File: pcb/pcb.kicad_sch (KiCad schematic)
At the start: 0 parts

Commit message: usbc almost done
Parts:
- added J1: TYPE-C-31-M-31, Andrews_Library:LCSC_SMD_USBC_C2760486, symbol Andrews_Library:LCSC_SMD_USBC_C2760486
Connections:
- no-connect marks 0 -> 13
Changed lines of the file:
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@@
 		(company "Andrew Cromar")
+	)
+	(no_connect
+		(at 139.7 88.9)
+	)
+	(no_connect
+		(at 128.27 80.01)
+	)
+	(no_connect
+		(at 130.81 106.68)
+	)
+	(no_connect
+		(at 128.27 106.68)
+	)
+	(no_connect
+		(at 139.7 93.98)
+	)
+	(no_connect
+		(at 139.7 96.52)
+	)
+	(no_connect
+		(at 139.7 99.06)
+	)
+	(no_connect
+		(at 139.7 91.44)
+	)
+	(no_connect
+		(at 125.73 106.68)
+	)
+	(no_connect
+		(at 139.7 86.36)
+	)
+	(no_connect
+		(at 116.84 99.06)
+	)
+	(no_connect
+		(at 130.81 80.01)
+	)
+	(no_connect
+		(at 116.84 96.52)
+	)
+	(symbol
+		(lib_id "Andrews_Library:LCSC_SMD_USBC_C2760486")
+		(at 128.27 92.71 0)
+		(unit 1)
+		(body_style 1)
+		(exclude_from_sim no)
+		(in_bom yes)
+		(on_board yes)
+		(in_pos_files yes)
+		(dnp no)
+		(fields_autoplaced yes)
+		(property "Reference" "J1"
+			(at 132.9533 77.47 0)
+			(show_name no)
+			(do_not_autoplace no)
+			(effects
+				(font
+					(size 1.27 1.27)
+				)
+				(justify left)
+			)
+		)
+		(property "Value" "TYPE-C-31-M-31"
+			(at 132.9533 80.01 0)
+			(show_name no)
+			(do_not_autoplace no)
+			(effects
+				(font
+					(size 1.27 1.27)
+				)
+				(justify left)
+			)
+		)
+		(property "Footprint" "Andrews_Library:LCSC_SMD_USBC_C2760486"
+			(at 128.27 92.71 0)
+			(hide yes)
+			(show_name no)
+			(do_not_autoplace no)
+			(effects
+				(font
+					(size 1.27 1.27)
+				)
+			)
+		)
+		(property "Datasheet" "https://www.lcsc.com/datasheet/C2760486.pdf"
+			(at 128.27 92.71 0)
+			(hide yes)
+			(show_name no)
+			(do_not_autoplace no)
+			(effects
+				(font
+					(size 1.27 1.27)
+				)
+			)
+		)
+		(property "Description" ""
+			(at 128.27 92.71 0)
+			(hide yes)
+			(show_name no)
+			(do_not_autoplace no)
+			(effects
+				(font
+					(size 1.27 1.27)
+				)
+			)
+		)
+		(property "LCSC" "C2760486"
+			(at 128.27 92.71 0)
+			(hide yes)
+			(show_name no)
+			(do_not_autoplace no)
+			(effects
+				(font
+					(size 1.27 1.27)
+				)
+			)
+		)
+		(pin "A12"
+		)
+		(pin "B8"
+		)
+		(pin "A7"
+		)
+		(pin "A8"
+		)
+		(pin "A9"
+		)
+		(pin "B7"
+		)
+		(pin "B5"
+		)
+		(pin "B6"
+		)
+		(pin "A6"
+		)
+		(pin "A5"
+		)
+		(pin "A4"
+		)
+		(pin "A1"
+		)
+		(pin "1"
+		)
+		(instances
+			(project "pcb"
+				(path "/37969d75-6775-4969-b3c5-2af34bbf809f"
+					(reference "J1")
+					(unit 1)
+				)
+			)
+		)
 	)
 	(sheet_instances

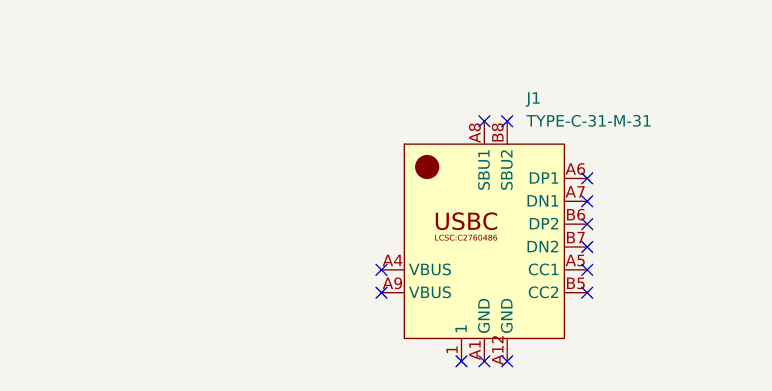
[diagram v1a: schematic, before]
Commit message: started working on voltage regulator
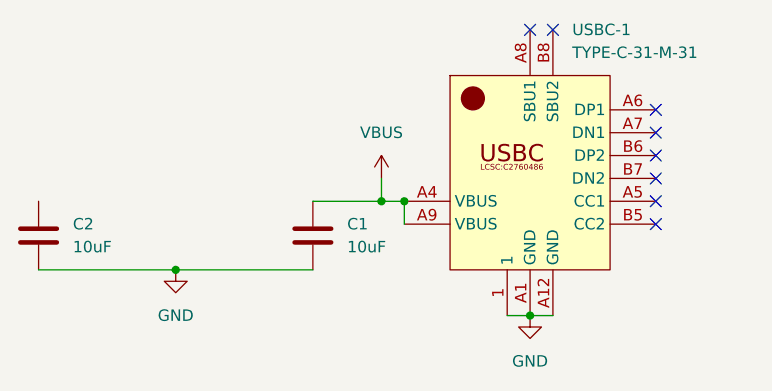
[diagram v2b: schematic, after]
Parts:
- removed J1: TYPE-C-31-M-31, Andrews_Library:LCSC_SMD_USBC_C2760486, symbol Andrews_Library:LCSC_SMD_USBC_C2760486
- added C1, C2: 10uF, symbol Device:C
- added USBC-1: TYPE-C-31-M-31, Andrews_Library:LCSC_SMD_USBC_C2760486, symbol Andrews_Library:LCSC_SMD_USBC_C2760486
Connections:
- new net GND: C1.2, C2.2, USBC-1.1, USBC-1.A1 (GND), USBC-1.A12 (GND)
- new net VBUS: C1.1, USBC-1.A4 (VBUS), USBC-1.A9 (VBUS)
- no-connect marks 13 -> 8

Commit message: please
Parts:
- added U1: 1117-3.3, symbol Andrews_Library:LCSC_SMD_1117-3.3v_C5125088
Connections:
- net GND: now also C1.1, U1.1 (GND/ADJ); no longer C1.2
- net VBUS: now also C1.2, U1.3 (VIN); no longer C1.1
- net at C2.1: now also U1.2 (VOUT), U1.4 (VOUT)
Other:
- moved on the sheet: C1, C2
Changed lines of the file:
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@@
+	)
+	(junction
+		(at 87.63 88.9)
+		(diameter 0)
+		(color 0 0 0 0)
+	)
+	(junction
+		(at 114.3 88.9)
+		(diameter 0)
+		(color 0 0 0 0)
 	)
 	(junction
@@
 	)
 	(junction
-		(at 93.98 96.52)
+		(at 97.79 96.52)
 		(diameter 0)
 		(color 0 0 0 0)
@@
 	(wire
 		(pts
-			(xy 93.98 96.52) (xy 109.22 96.52)
-		)
-		(stroke
-			(width 0)
-			(type default)
-		)
-	)
-	(wire
-		(pts
-			(xy 109.22 88.9) (xy 116.84 88.9)
-		)
-		(stroke
-			(width 0)
-			(type default)
-		)
-	)
-	(wire
-		(pts
-			(xy 119.38 88.9) (xy 116.84 88.9)
+			(xy 114.3 88.9) (xy 116.84 88.9)
+		)
+		(stroke
+			(width 0)
+			(type default)
+		)
+	)
+	(wire
+		(pts
+			(xy 97.79 96.52) (xy 114.3 96.52)
+		)
+		(stroke
+			(width 0)
+			(type default)
+		)
+	)
+	(wire
+		(pts
+			(xy 87.63 88.9) (xy 87.63 90.17)
+		)
+		(stroke
+			(width 0)
+			(type default)
+		)
+	)
+	(wire
+		(pts
+			(xy 87.63 87.63) (xy 87.63 88.9)
+		)
+		(stroke
+			(width 0)
+			(type default)
+		)
+	)
+	(wire
+		(pts
+			(xy 80.01 88.9) (xy 87.63 88.9)
+		)
+		(stroke
+			(width 0)
+			(type default)
+		)
+	)
+	(wire
+		(pts
+			(xy 97.79 93.98) (xy 97.79 96.52)
+		)
+		(stroke
+			(width 0)
+			(type default)
+		)
+	)
+	(wire
+		(pts
+			(xy 116.84 88.9) (xy 119.38 88.9)
 		)
 		(stroke
@@
 	(wire
 		(pts
-			(xy 78.74 96.52) (xy 93.98 96.52)
+			(xy 80.01 96.52) (xy 97.79 96.52)
+		)
+		(stroke
+			(width 0)
+			(type default)
+		)
+	)
+	(wire
+		(pts
+			(xy 106.68 88.9) (xy 114.3 88.9)
 		)
 		(stroke
@@
 	)
 	(symbol
+		(lib_id "Andrews_Library:LCSC_SMD_1117-3.3v_C5125088")
+		(at 97.79 83.82 0)
+		(mirror y)
+		(unit 1)
+		(body_style 1)
+		(exclude_from_sim no)
+		(in_bom yes)
+		(on_board yes)
+		(in_pos_files yes)
+		(dnp no)
+		(fields_autoplaced yes)
+		(property "Reference" "U1"
+			(at 97.155 71.12 0)
+			(show_name no)
+			(do_not_autoplace no)
+			(effects
+				(font
+					(size 1.27 1.27)
+				)
+			)
+		)
+		(property "Value" "1117-3.3"
+			(at 97.155 73.66 0)
+			(show_name no)
+			(do_not_autoplace no)
+			(effects
+				(font
+					(size 1.27 1.27)
+				)
+			)
+		)
+		(property "Footprint" ""
+			(at 101.6 78.74 0)
+			(hide yes)
+			(show_name no)
+			(do_not_autoplace no)
+			(effects
+				(font
+					(size 1.27 1.27)
+				)
+			)
+		)
+		(property "Datasheet" "https://www.lcsc.com/datasheet/C5125088.pdf"
+			(at 97.79 83.82 0)
+			(hide yes)
+			(show_name no)
+			(do_not_autoplace no)
+			(effects
+				(font
+					(size 1.27 1.27)
+				)
+			)
+		)
+		(property "Description" ""
+			(at 101.6 78.74 0)
+			(hide yes)
+			(show_name no)
+			(do_not_autoplace no)
+			(effects
+				(font
+					(size 1.27 1.27)
+				)
+			)
+		)
+		(property "LCSC" "C5125088"
+			(at 97.79 83.82 0)
+			(hide yes)
+			(show_name no)
+			(do_not_autoplace no)
+			(effects
+				(font
+					(size 1.27 1.27)
+				)
+			)
+		)
+		(pin "1"
+		)
+		(pin "4"
+		)
+		(pin "3"
+		)
+		(pin "2"
+		)
+		(instances
+			(project "pcb"
+				(path "/37969d75-6775-4969-b3c5-2af34bbf809f"
+					(reference "U1")
+					(unit 1)
+				)
+			)
+		)
+	)
+	(symbol
 		(lib_id "power:GND")
 		(at 133.35 101.6 0)
@@
 	(symbol
 		(lib_id "Device:C")
-		(at 109.22 92.71 0)
+		(at 114.3 92.71 0)
+		(mirror x)
 		(unit 1)
 		(body_style 1)
@@
 		(in_pos_files yes)
 		(dnp no)
-		(fields_autoplaced yes)
 		(property "Reference" "C1"
-			(at 113.03 91.4399 0)
-			(show_name no)
-			(do_not_autoplace no)
-			(effects
-				(font
-					(size 1.27 1.27)
-				)
-				(justify left)
+			(at 110.49 91.4399 0)
+			(show_name no)
+			(do_not_autoplace no)
+			(effects
+				(font
+					(size 1.27 1.27)
+				)
+				(justify right)
 			)
 		)
 		(property "Value" "10uF"
-			(at 113.03 93.9799 0)
-			(show_name no)
-			(do_not_autoplace no)
-			(effects
-				(font
-					(size 1.27 1.27)
-				)
-				(justify left)
+			(at 110.49 93.9799 0)
+			(show_name no)
+			(do_not_autoplace no)
+			(effects
+				(font
+					(size 1.27 1.27)
+				)
+				(justify right)
 			)
 		)
 		(property "Footprint" ""
-			(at 110.1852 96.52 0)
+			(at 115.2652 88.9 0)
 			(hide yes)
 			(show_name no)
@@
 		)
 		(property "Datasheet" ""
-			(at 109.22 92.71 0)
+			(at 114.3 92.71 0)
 			(hide yes)
 			(show_name no)
@@
 		)
 		(property "Description" "Unpolarized capacitor"
-			(at 109.22 92.71 0)
+			(at 114.3 92.71 0)
 			(hide yes)
 			(show_name no)
@@
 	(symbol
 		(lib_id "power:GND")
-		(at 93.98 96.52 0)
+		(at 97.79 96.52 0)
 		(unit 1)
 		(body_style 1)
@@
 		(fields_autoplaced yes)
 		(property "Reference" "#PWR03"
-			(at 93.98 102.87 0)
+			(at 97.79 102.87 0)
 			(hide yes)
 			(show_name no)
@@
 		)
 		(property "Value" "GND"
-			(at 93.98 101.6 0)
+			(at 97.79 101.6 0)
 			(show_name no)
 			(do_not_autoplace no)
@@
 		)
 		(property "Footprint" ""
-			(at 93.98 96.52 0)
+			(at 97.79 96.52 0)
 			(hide yes)
 			(show_name no)
@@
 		)
 		(property "Datasheet" ""
-			(at 93.98 96.52 0)
+			(at 97.79 96.52 0)
 			(hide yes)
 			(show_name no)
@@
 		)
 		(property "Description" "Power symbol creates a global label with name \"GND\" , ground"
-			(at 93.98 96.52 0)
+			(at 97.79 96.52 0)
 			(hide yes)
 			(show_name no)
@@
 	(symbol
 		(lib_id "Device:C")
-		(at 78.74 92.71 0)
+		(at 80.01 92.71 0)
 		(unit 1)
 		(body_style 1)
@@
 		(fields_autoplaced yes)
 		(property "Reference" "C2"
-			(at 82.55 91.4399 0)
+			(at 83.82 91.4399 0)
 			(show_name no)
 			(do_not_autoplace no)
@@
 		)
 		(property "Value" "10uF"
-			(at 82.55 93.9799 0)
+			(at 83.82 93.9799 0)
 			(show_name no)
 			(do_not_autoplace no)
@@
 		)
 		(property "Footprint" ""
-			(at 79.7052 96.52 0)
+			(at 80.9752 96.52 0)
 			(hide yes)
 			(show_name no)
@@
 		)
 		(property "Datasheet" ""
-			(at 78.74 92.71 0)
+			(at 80.01 92.71 0)
 			(hide yes)
 			(show_name no)
@@
 		)
 		(property "Description" "Unpolarized capacitor"
-			(at 78.74 92.71 0)
-			(hide yes)
-			(show_name no)
+			(at 80.01 92.71 0)
+			(hide yes)
+			(show_name no)

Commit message: added it to the pcb
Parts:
- U1: footprint (none) -> Andrews_Library:LCSC_SMD_1117-3.3v_C5125088
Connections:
- net VBUS: now also U1.2 (VOUT); no longer U1.3 (VIN)
- new net: C2.1, U1.3 (VIN)
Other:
- moved on the sheet: C2
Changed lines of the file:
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@@
 	)
 	(junction
-		(at 87.63 88.9)
+		(at 119.38 88.9)
+		(diameter 0)
+		(color 0 0 0 0)
+	)
+	(junction
+		(at 97.79 96.52)
 		(diameter 0)
 		(color 0 0 0 0)
@@
 	)
 	(junction
-		(at 119.38 88.9)
-		(diameter 0)
-		(color 0 0 0 0)
-	)
-	(junction
-		(at 97.79 96.52)
-		(diameter 0)
-		(color 0 0 0 0)
-	)
-	(junction
 		(at 133.35 101.6)
 		(diameter 0)
@@
 	(wire
 		(pts
+			(xy 82.55 88.9) (xy 88.9 88.9)
+		)
+		(stroke
+			(width 0)
+			(type default)
+		)
+	)
+	(wire
+		(pts
 			(xy 130.81 101.6) (xy 133.35 101.6)
 		)
@@
 	(wire
 		(pts
-			(xy 87.63 88.9) (xy 87.63 90.17)
-		)
-		(stroke
-			(width 0)
-			(type default)
-		)
-	)
-	(wire
-		(pts
-			(xy 87.63 87.63) (xy 87.63 88.9)
-		)
-		(stroke
-			(width 0)
-			(type default)
-		)
-	)
-	(wire
-		(pts
-			(xy 80.01 88.9) (xy 87.63 88.9)
-		)
-		(stroke
-			(width 0)
-			(type default)
-		)
-	)
-	(wire
-		(pts
 			(xy 97.79 93.98) (xy 97.79 96.52)
 		)
@@
 	(wire
 		(pts
-			(xy 80.01 96.52) (xy 97.79 96.52)
-		)
-		(stroke
-			(width 0)
-			(type default)
-		)
-	)
-	(wire
-		(pts
-			(xy 106.68 88.9) (xy 114.3 88.9)
+			(xy 107.95 88.9) (xy 114.3 88.9)
+		)
+		(stroke
+			(width 0)
+			(type default)
+		)
+	)
+	(wire
+		(pts
+			(xy 82.55 96.52) (xy 97.79 96.52)
 		)
 		(stroke
@@
 	)
 	(symbol
-		(lib_id "Andrews_Library:LCSC_SMD_1117-3.3v_C5125088")
-		(at 97.79 83.82 0)
-		(mirror y)
-		(unit 1)
-		(body_style 1)
-		(exclude_from_sim no)
-		(in_bom yes)
-		(on_board yes)
-		(in_pos_files yes)
-		(dnp no)
-		(fields_autoplaced yes)
-		(property "Reference" "U1"
-			(at 97.155 71.12 0)
-			(show_name no)
-			(do_not_autoplace no)
-			(effects
-				(font
-					(size 1.27 1.27)
-				)
-			)
-		)
-		(property "Value" "1117-3.3"
-			(at 97.155 73.66 0)
-			(show_name no)
-			(do_not_autoplace no)
-			(effects
-				(font
-					(size 1.27 1.27)
-				)
-			)
-		)
-		(property "Footprint" ""
-			(at 101.6 78.74 0)
-			(hide yes)
-			(show_name no)
-			(do_not_autoplace no)
-			(effects
-				(font
-					(size 1.27 1.27)
-				)
-			)
-		)
-		(property "Datasheet" "https://www.lcsc.com/datasheet/C5125088.pdf"
-			(at 97.79 83.82 0)
-			(hide yes)
-			(show_name no)
-			(do_not_autoplace no)
-			(effects
-				(font
-					(size 1.27 1.27)
-				)
-			)
-		)
-		(property "Description" ""
-			(at 101.6 78.74 0)
-			(hide yes)
-			(show_name no)
-			(do_not_autoplace no)
-			(effects
-				(font
-					(size 1.27 1.27)
-				)
-			)
-		)
-		(property "LCSC" "C5125088"
-			(at 97.79 83.82 0)
-			(hide yes)
-			(show_name no)
-			(do_not_autoplace no)
-			(effects
-				(font
-					(size 1.27 1.27)
-				)
-			)
-		)
-		(pin "1"
-		)
-		(pin "4"
-		)
-		(pin "3"
-		)
-		(pin "2"
-		)
-		(instances
-			(project "pcb"
-				(path "/37969d75-6775-4969-b3c5-2af34bbf809f"
-					(reference "U1")
-					(unit 1)
-				)
-			)
-		)
-	)
-	(symbol
 		(lib_id "power:GND")
 		(at 133.35 101.6 0)
@@
 	)
 	(symbol
+		(lib_id "Andrews_Library:LCSC_SMD_1117-3.3v_C5125088")
+		(at 97.79 83.82 0)
+		(unit 1)
+		(body_style 1)
+		(exclude_from_sim no)
+		(in_bom yes)
+		(on_board yes)
+		(in_pos_files yes)
+		(dnp no)
+		(fields_autoplaced yes)
+		(property "Reference" "U1"
+			(at 98.425 71.12 0)
+			(show_name no)
+			(do_not_autoplace no)
+			(effects
+				(font
+					(size 1.27 1.27)
+				)
+			)
+		)
+		(property "Value" "1117-3.3"
+			(at 98.425 73.66 0)
+			(show_name no)
+			(do_not_autoplace no)
+			(effects
+				(font
+					(size 1.27 1.27)
+				)
+			)
+		)
+		(property "Footprint" "Andrews_Library:LCSC_SMD_1117-3.3v_C5125088"
+			(at 97.79 83.82 0)
+			(hide yes)
+			(show_name no)
+			(do_not_autoplace no)
+			(effects
+				(font
+					(size 1.27 1.27)
+				)
+			)
+		)
+		(property "Datasheet" "https://www.lcsc.com/datasheet/C5125088.pdf"
+			(at 97.79 83.82 0)
+			(hide yes)
+			(show_name no)
+			(do_not_autoplace no)
+			(effects
+				(font
+					(size 1.27 1.27)
+				)
+			)
+		)
+		(property "Description" ""
+			(at 93.98 78.74 0)
+			(hide yes)
+			(show_name no)
+			(do_not_autoplace no)
+			(effects
+				(font
+					(size 1.27 1.27)
+				)
+			)
+		)
+		(property "LCSC" "C5125088"
+			(at 97.79 83.82 0)
+			(hide yes)
+			(show_name no)
+			(do_not_autoplace no)
+			(effects
+				(font
+					(size 1.27 1.27)
+				)
+			)
+		)
+		(pin "2"
+		)
+		(pin "3"
+		)
+		(pin "1"
+		)
+		(instances
+			(project "pcb"
+				(path "/37969d75-6775-4969-b3c5-2af34bbf809f"
+					(reference "U1")
+					(unit 1)
+				)
+			)
+		)
+	)
+	(symbol
 		(lib_id "power:GND")
 		(at 97.79 96.52 0)
@@
 	(symbol
 		(lib_id "Device:C")
-		(at 80.01 92.71 0)
+		(at 82.55 92.71 0)
 		(unit 1)
 		(body_style 1)
@@
 		(fields_autoplaced yes)
 		(property "Reference" "C2"
-			(at 83.82 91.4399 0)
+			(at 86.36 91.4399 0)
 			(show_name no)
 			(do_not_autoplace no)
@@
 		)
 		(property "Value" "10uF"
-			(at 83.82 93.9799 0)
+			(at 86.36 93.9799 0)
 			(show_name no)
 			(do_not_autoplace no)
@@
 		)
 		(property "Footprint" ""
-			(at 80.9752 96.52 0)
+			(at 83.5152 96.52 0)
 			(hide yes)
 			(show_name no)
@@
 		)
 		(property "Datasheet" ""
-			(at 80.01 92.71 0)
+			(at 82.55 92.71 0)
 			(hide yes)
 			(show_name no)
@@
 		)
 		(property "Description" "Unpolarized capacitor"
-			(at 80.01 92.71 0)
-			(hide yes)
-			(show_name no)
+			(at 82.55 92.71 0)
+			(hide yes)
+			(show_name no)

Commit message: added footprints to c
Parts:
- C1, C2: footprint (none) -> Capacitor_SMD:C_0201_0603Metric; LCSC (none) -> C1691
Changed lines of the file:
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@@
 			)
 		)
-		(property "Footprint" ""
+		(property "Footprint" "Capacitor_SMD:C_0201_0603Metric"
 			(at 115.2652 88.9 0)
 			(hide yes)
@@
 		)
 		(property "Description" "Unpolarized capacitor"
+			(at 114.3 92.71 0)
+			(hide yes)
+			(show_name no)
+			(do_not_autoplace no)
+			(effects
+				(font
+					(size 1.27 1.27)
+				)
+			)
+		)
+		(property "LCSC" "C1691"
 			(at 114.3 92.71 0)
 			(hide yes)
@@
 			)
 		)
-		(property "Footprint" ""
+		(property "Footprint" "Capacitor_SMD:C_0201_0603Metric"
 			(at 83.5152 96.52 0)
 			(hide yes)
@@
 			(at 82.55 92.71 0)
 			(hide yes)
+			(show_name no)
+			(do_not_autoplace no)
+			(effects
+				(font
+					(size 1.27 1.27)
+				)
+			)
+		)
+		(property "LCSC" "C1691"
+			(at 82.55 92.71 0)
+			(hide yes)

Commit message: usbc schematic done?
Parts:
- added R1, R2: 27, Resistor_SMD:R_0201_0603Metric, symbol Device:R
- added R3, R4: 5.1k, Resistor_SMD:R_0201_0603Metric, symbol Device:R
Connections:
- net GND: now also R3.2, R4.2
- net at USBC-1.A5 (CC1): now also R3.1
- net at USBC-1.A6 (DP1): now also USBC-1.B6 (DP2), R1.1
- net at USBC-1.A7 (DN1): now also USBC-1.B7 (DN2), R2.1
- net at USBC-1.B5 (CC2): now also R4.1
- new net USB_DN: R2.2
- new net USB_DP: R1.2
- no-connect marks 8 -> 2

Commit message: fixxed usbc stuff
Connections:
- net GND: now also USBC-1.A1/B12 (GND), USBC-1.B1/A12 (GND); no longer USBC-1.A1 (GND), USBC-1.A12 (GND)
- net VBUS: now also USBC-1.A4/B9 (VBUS), USBC-1.B4/A9 (VBUS); no longer USBC-1.A4 (VBUS), USBC-1.A9 (VBUS)
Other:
- moved on the sheet: C1, C2, R1, R2, R3, R4, U1, USBC-1
